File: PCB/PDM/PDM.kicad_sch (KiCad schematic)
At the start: 11 parts, among them IC4 TS5A21366DCUR, IC5 TMP126NDCKR, IC6 TMP126NDCKR, U2 MCP2561-E-SN, U3 MCP2561-E-SN

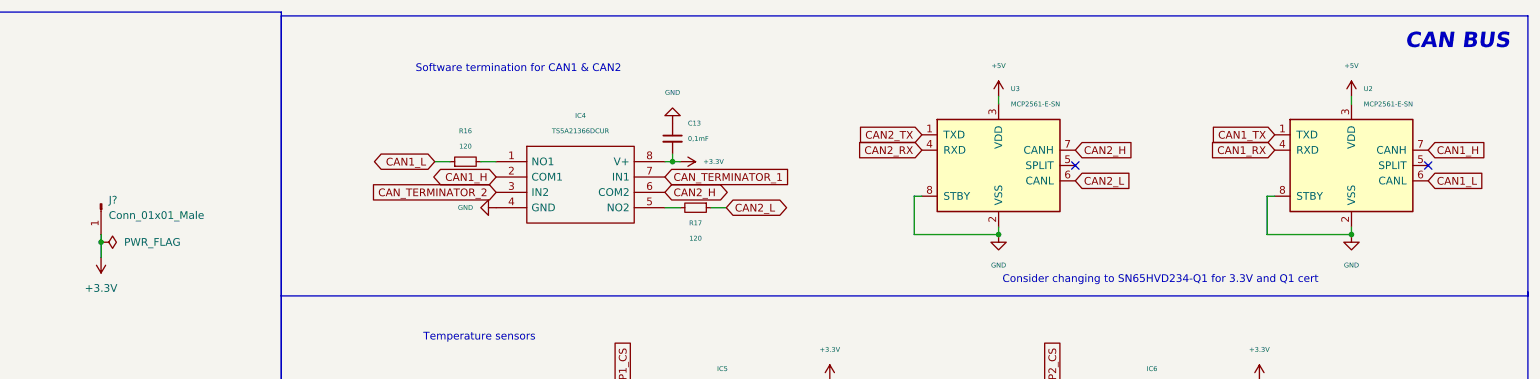
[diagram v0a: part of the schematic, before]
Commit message: Changed MCP2561 to SN65HVD230 for Q1 and 3.3V supply
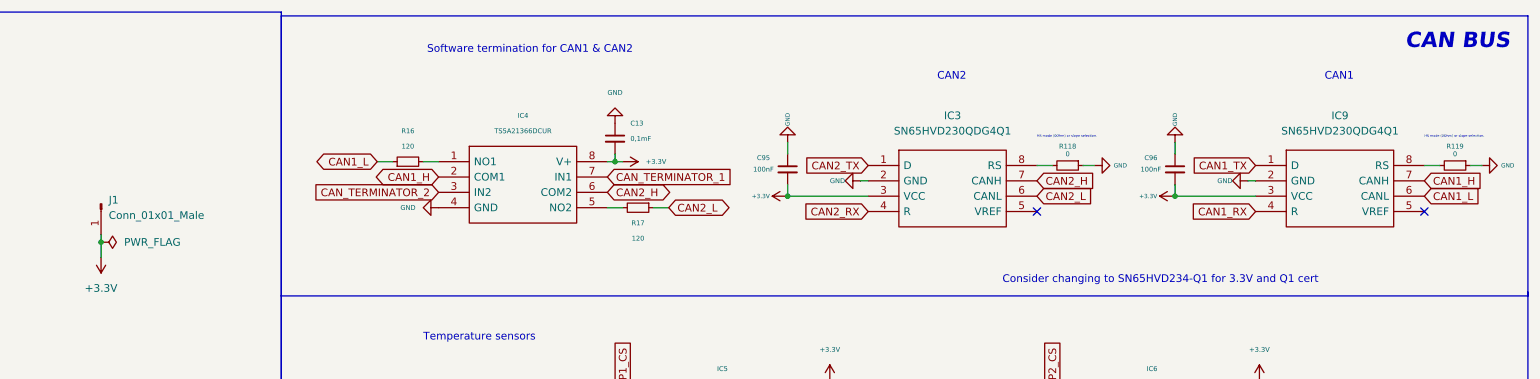
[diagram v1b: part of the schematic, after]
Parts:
- removed U2, U3: MCP2561-E-SN, Package_SO:SOIC-8_3.9x4.9mm_P1.27mm, symbol Interface_CAN_LIN:MCP2561-E-SN
- added C95, C96: 100nF, Capacitor_SMD:C_0805_2012Metric, symbol Device:C_Small
- added IC3, IC9: SN65HVD230QDG4Q1, PDM_Additional:SOIC127P600X175-8N, symbol PDM_additional:SN65HVD230QDG4Q1
- added R118, R119: 0, Resistor_SMD:R_0402_1005Metric, symbol Device:R_Small
- gave numbers to parts that had none: 1
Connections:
- net +3.3V: now also C95.2, C96.2, IC3.3 (VCC), IC9.3 (VCC)
- net CAN1_H: now also IC9.7 (CANH)
- net CAN1_L: now also IC9.6 (CANL)
- net CAN1_RX: now also IC9.4 (R)
- net CAN1_TX: now also IC9.1 (D)
- net CAN2_H: now also IC3.7 (CANH)
- net CAN2_L: now also IC3.6 (CANL)
- net CAN2_RX: now also IC3.4 (R)
- net CAN2_TX: now also IC3.1 (D)
- net GND: now also C95.1, C96.1, IC3.2 (GND), IC9.2 (GND), R118.1, R119.1
- new net: IC3.8 (RS), R118.2
- new net: IC9.8 (RS), R119.2
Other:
- note added: "CAN1"
- note added: "CAN2"
- note added: "HS mode (0Ohm) or slope selection."
- moved on the sheet: C13, IC4, R16, R17

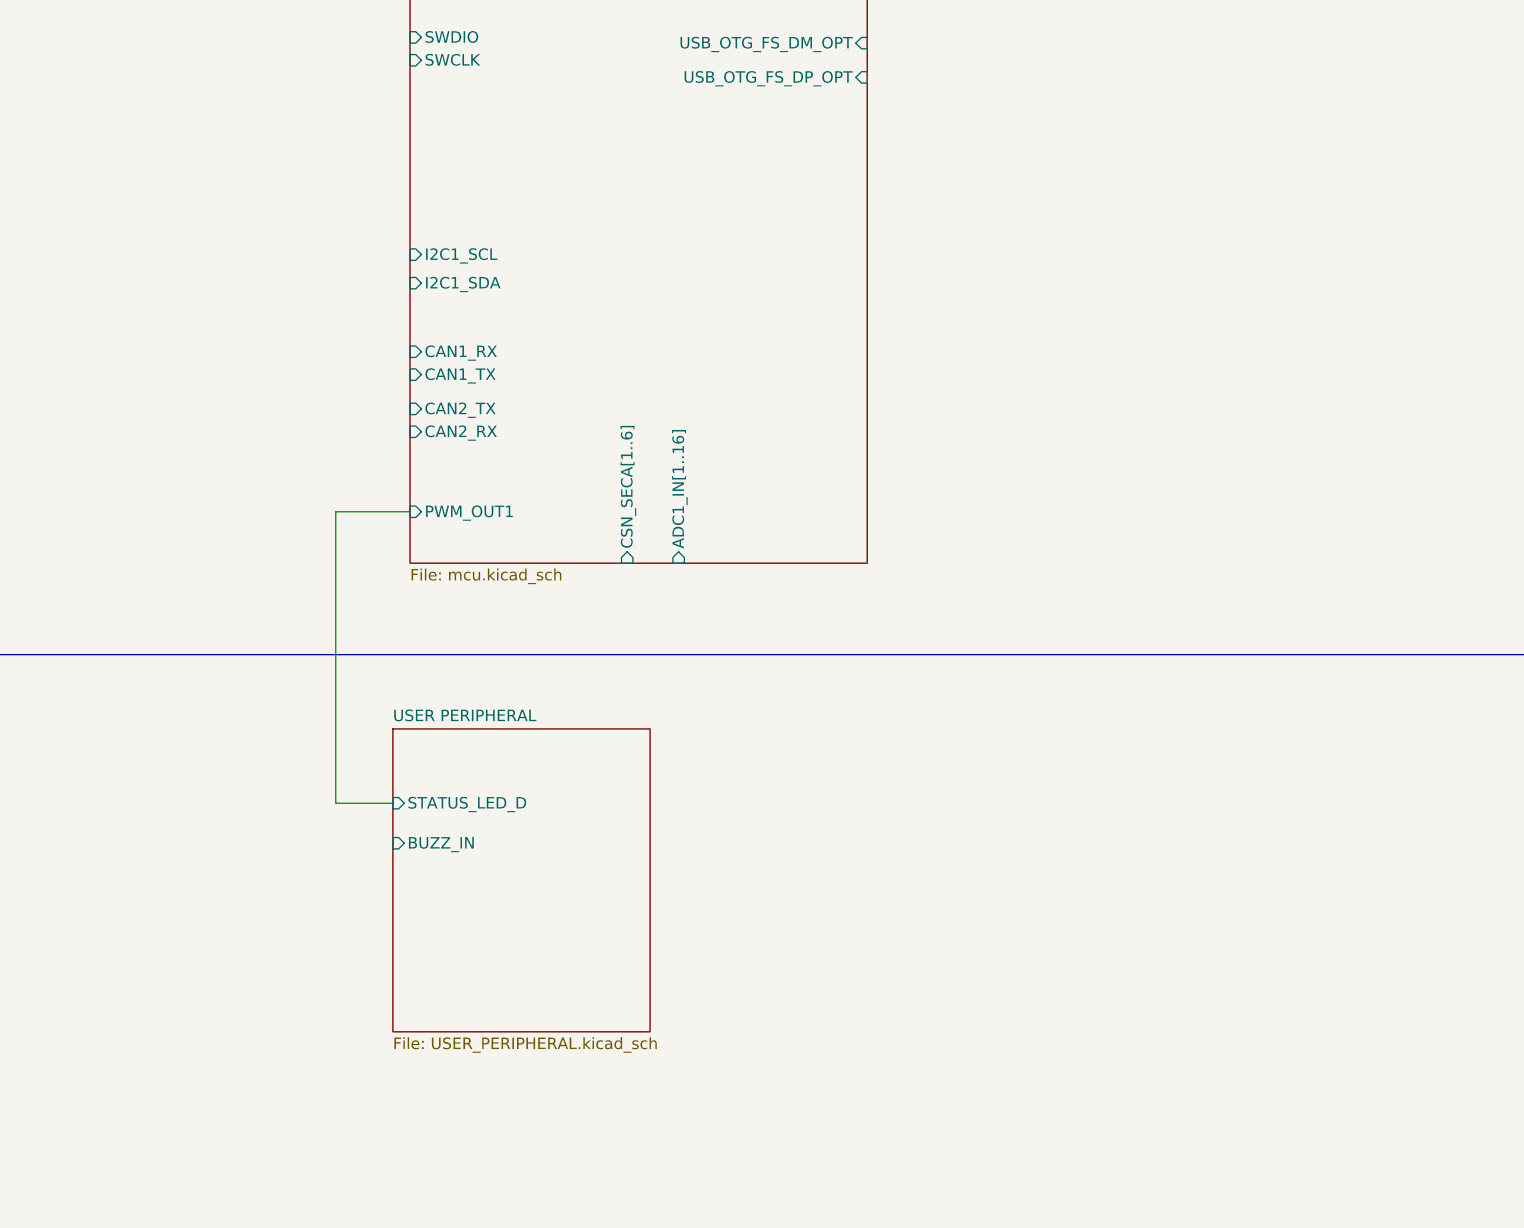
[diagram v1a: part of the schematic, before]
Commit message: Added TE Superseal 1.0 connector 60 pins
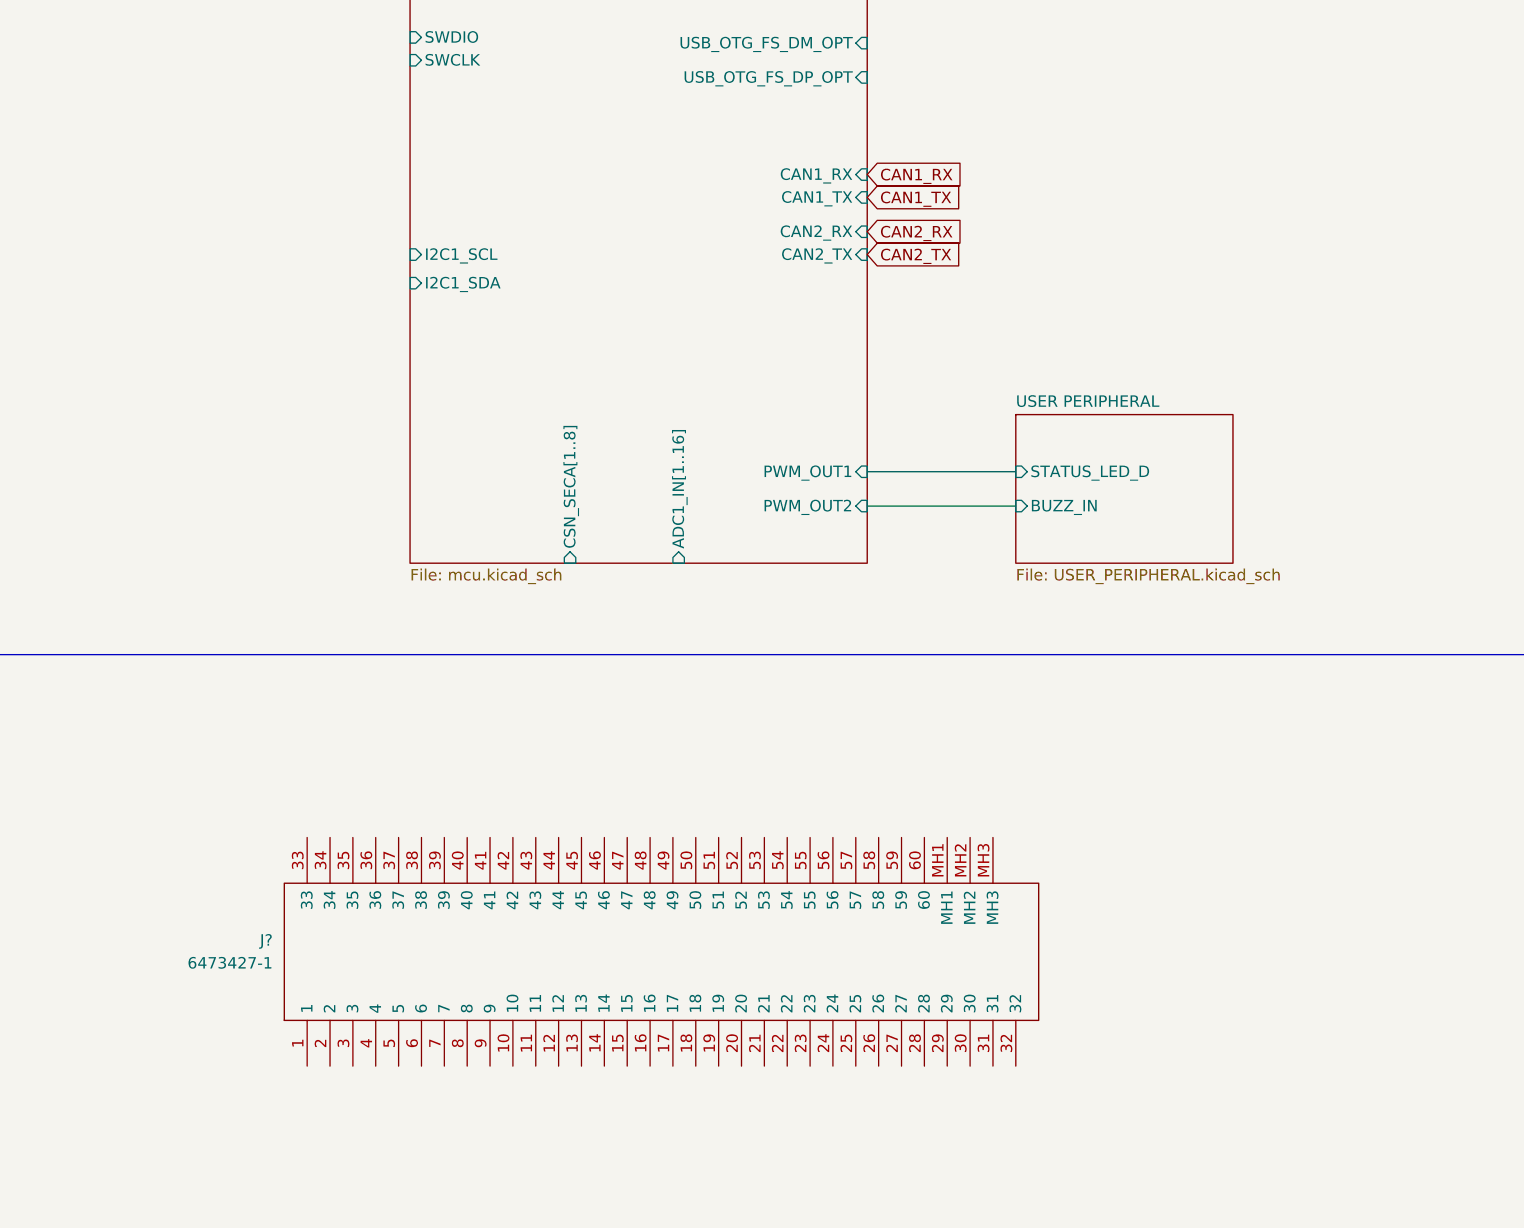
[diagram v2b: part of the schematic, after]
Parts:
- added J?: 6473427-1, 64734271, symbol PDM_additional:6473427-1
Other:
- sheet MCU ports: added CSN_SECA[1..8], PWM_OUT2; removed CSN_SECA[1..6]
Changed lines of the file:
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@@
+    (stroke (width 0) (type default) (color 0 0 0 0))
+  )
+  (wire (pts (xy 326.39 168.91) (xy 342.9 168.91))
     (stroke (width 0) (type default) (color 0 0 0 0))
   )
@@
     (stroke (width 0) (type default) (color 0 0 0 0))
   )
+  (wire (pts (xy 326.39 172.72) (xy 342.9 172.72))
+    (stroke (width 0) (type default) (color 0 0 0 0))
+  )
   (polyline (pts (xy 407.67 103.505) (xy 407.67 57.785))
     (stroke (width 0) (type default) (color 0 0 0 0))
@@
     (stroke (width 0) (type default) (color 0 0 0 0))
   )
-  (wire (pts (xy 273.685 205.74) (xy 267.335 205.74))
-    (stroke (width 0) (type default) (color 0 0 0 0))
-  )
   (wire (pts (xy 48.895 38.735) (xy 60.96 38.735))
     (stroke (width 0) (type default) (color 0 0 0 0))
@@
     (stroke (width 0) (type default) (color 0 0 0 0))
   )
-  (wire (pts (xy 267.335 205.74) (xy 267.335 173.355))
-    (stroke (width 0) (type default) (color 0 0 0 0))
-  )
   (polyline (pts (xy 201.295 285.115) (xy 12.065 285.115))
     (stroke (width 0) (type default) (color 0 0 0 0))
@@
   )
   (polyline (pts (xy 201.295 189.23) (xy 407.67 189.23))
-    (stroke (width 0) (type default) (color 0 0 0 0))
-  )
-  (wire (pts (xy 267.335 173.355) (xy 275.59 173.355))
     (stroke (width 0) (type default) (color 0 0 0 0))
   )
@@
     )
   )
+  (global_label "CAN2_RX" (shape input) (at 326.39 142.24 0) (fields_autoplaced)
+    (effects (font (size 1.27 1.27)) (justify left))
+    (property "Intersheet References" "${INTERSHEET_REFS}" (id 0) (at 337.1488 142.3194 0)
+      (effects (font (size 1.27 1.27)) (justify left) hide)
+    )
+  )
   (global_label "TEMP2_ALERT" (shape input) (at 367.03 81.28 0) (fields_autoplaced)
     (effects (font (size 1.27 1.27)) (justify left))
     (property "Intersheet References" "${INTERSHEET_REFS}" (id 0) (at 381.9617 81.2006 0)
+      (effects (font (size 1.27 1.27)) (justify left) hide)
+    )
+  )
+  (global_label "CAN1_TX" (shape input) (at 326.39 138.43 0) (fields_autoplaced)
+    (effects (font (size 1.27 1.27)) (justify left))
+    (property "Intersheet References" "${INTERSHEET_REFS}" (id 0) (at 336.8464 138.5094 0)
       (effects (font (size 1.27 1.27)) (justify left) hide)
     )
@@
     )
   )
+  (global_label "CAN1_RX" (shape input) (at 326.39 135.89 0) (fields_autoplaced)
+    (effects (font (size 1.27 1.27)) (justify left))
+    (property "Intersheet References" "${INTERSHEET_REFS}" (id 0) (at 337.1488 135.9694 0)
+      (effects (font (size 1.27 1.27)) (justify left) hide)
+    )
+  )
   (global_label "CAN1_TX" (shape input) (at 362.585 36.83 180) (fields_autoplaced)
     (effects (font (size 1.27 1.27)) (justify right))
@@
     (effects (font (size 1.27 1.27)) (justify left))
     (property "Intersheet References" "${INTERSHEET_REFS}" (id 0) (at 310.8417 81.2006 0)
+      (effects (font (size 1.27 1.27)) (justify left) hide)
+    )
+  )
+  (global_label "CAN2_TX" (shape input) (at 326.39 144.78 0) (fields_autoplaced)
+    (effects (font (size 1.27 1.27)) (justify left))
+    (property "Intersheet References" "${INTERSHEET_REFS}" (id 0) (at 336.8464 144.8594 0)
       (effects (font (size 1.27 1.27)) (justify left) hide)
     )
@@
     (pin "2")
   )
+  (symbol (lib_id "PDM_additional:6473427-1") (at 264.16 234.95 90) (unit 1)
+    (in_bom yes) (on_board yes) (fields_autoplaced)
+    (property "Reference" "J?" (id 0) (at 260.35 220.9799 90)
+      (effects (font (size 1.27 1.27)) (justify left))
+    )
+    (property "Value" "6473427-1" (id 1) (at 260.35 223.5199 90)
+      (effects (font (size 1.27 1.27)) (justify left))
+    )
+    (property "Footprint" "64734271" (id 2) (at 261.62 213.36 0)
+      (effects (font (size 1.27 1.27)) (justify left) hide)
+    )
+    (property "Datasheet" "https://www.te.com/commerce/DocumentDelivery/DDEController?Action=showdoc&DocId=Customer+Drawing%7F9-1437287-8%7FA1%7Fpdf%7FEnglish%7FENG_CD_9-1437287-8_A1.pdf%7F6473427-1" (id 3) (at 264.16 213.36 0)
+      (effects (font (size 1.27 1.27)) (justify left) hide)
+    )
+    (property "Description" "Automotive Connectors SUPER SEAL 60POS CAP ASY H AU" (id 4) (at 266.7 213.36 0)
+      (effects (font (size 1.27 1.27)) (justify left) hide)
+    )
+    (property "Height" "27.4" (id 5) (at 269.24 213.36 0)
+      (effects (font (size 1.27 1.27)) (justify left) hide)
+    )
+    (property "Manufacturer_Name" "TE Connectivity" (id 6) (at 271.78 213.36 0)
+      (effects (font (size 1.27 1.27)) (justify left) hide)
+    )
+    (property "Manufacturer_Part_Number" "6473427-1" (id 7) (at 274.32 213.36 0)
+      (effects (font (size 1.27 1.27)) (justify left) hide)
+    )
+    (property "Mouser Part Number" "571-6473427-1" (id 8) (at 276.86 213.36 0)
+      (effects (font (size 1.27 1.27)) (justify left) hide)
+    )
+    (property "Mouser Price/Stock" "https://www.mouser.co.uk/ProductDetail/TE-Connectivity/6473427-1?qs=%252BJ%252BJwDEtia0S2ZPotWhzbA%3D%3D" (id 9) (at 279.4 213.36 0)
+      (effects (font (size 1.27 1.27)) (justify left) hide)
+    )
+    (property "Arrow Part Number" "6473427-1" (id 10) (at 281.94 213.36 0)
+      (effects (font (size 1.27 1.27)) (justify left) hide)
+    )
+    (property "Arrow Price/Stock" "https://www.arrow.com/en/products/6473427-1/te-connectivity?region=nac" (id 11) (at 284.48 213.36 0)
+      (effects (font (size 1.27 1.27)) (justify left) hide)
+    )
+    (property "Mouser Testing Part Number" "" (id 12) (at 287.02 213.36 0)
+      (effects (font (size 1.27 1.27)) (justify left) hide)
+    )
+    (property "Mouser Testing Price/Stock" "" (id 13) (at 289.56 213.36 0)
+      (effects (font (size 1.27 1.27)) (justify left) hide)
+    )
+    (pin "1")
+    (pin "10")
+    (pin "11")
+    (pin "12")
+    (pin "13")
+    (pin "14")
+    (pin "15")
+    (pin "16")
+    (pin "17")
+    (pin "18")
+    (pin "19")
+    (pin "2")
+    (pin "20")
+    (pin "21")
+    (pin "22")
+    (pin "23")
+    (pin "24")
+    (pin "25")
+    (pin "26")
+    (pin "27")
+    (pin "28")
+    (pin "29")
+    (pin "3")
+    (pin "30")
+    (pin "31")
+    (pin "32")
+    (pin "33")
+    (pin "34")
+    (pin "35")
+    (pin "36")
+    (pin "37")
+    (pin "38")
+    (pin "39")
+    (pin "4")
+    (pin "40")
+    (pin "41")
+    (pin "42")
+    (pin "43")
+    (pin "44")
+    (pin "45")
+    (pin "46")
+    (pin "47")
+    (pin "48")
+    (pin "49")
+    (pin "5")
+    (pin "50")
+    (pin "51")
+    (pin "52")
+    (pin "53")
+    (pin "54")
+    (pin "55")
+    (pin "56")
+    (pin "57")
+    (pin "58")
+    (pin "59")
+    (pin "6")
+    (pin "60")
+    (pin "7")
+    (pin "8")
+    (pin "9")
+    (pin "MH1")
+    (pin "MH2")
+    (pin "MH3")
+  )
   (symbol (lib_id "power:PWR_FLAG") (at 171.45 49.53 270) (unit 1)
     (in_bom yes) (on_board yes) (fields_autoplaced)
@@
     )
   )
-  (sheet (at 273.685 197.485) (size 28.575 33.655) (fields_autoplaced)
+  (sheet (at 342.9 162.56) (size 24.13 16.51) (fields_autoplaced)
     (stroke (width 0.1524) (type solid) (color 0 0 0 0))
     (fill (color 0 0 0 0.0000))
-    (property "Sheet name" "USER PERIPHERAL" (id 0) (at 273.685 196.7734 0)
+    (property "Sheet name" "USER PERIPHERAL" (id 0) (at 342.9 161.8484 0)
       (effects (font (size 1.27 1.27)) (justify left bottom))
     )
-    (property "Sheet file" "USER_PERIPHERAL.kicad_sch" (id 1) (at 273.685 231.7246 0)
+    (property "Sheet file" "USER_PERIPHERAL.kicad_sch" (id 1) (at 342.9 179.6546 0)
       (effects (font (size 1.27 1.27)) (justify left top))
     )
-    (pin "STATUS_LED_D" input (at 273.685 205.74 180)
-      (effects (font (size 1.27 1.27)) (justify left))
-    )
-    (pin "BUZZ_IN" input (at 273.685 210.185 180)
+    (pin "STATUS_LED_D" input (at 342.9 168.91 180)
+      (effects (font (size 1.27 1.27)) (justify left))
+    )
+    (pin "BUZZ_IN" input (at 342.9 172.72 180)
       (effects (font (size 1.27 1.27)) (justify left))
     )
@@
       (effects (font (size 1.27 1.27)) (justify left))
     )
-    (pin "CAN1_RX" input (at 275.59 155.575 180)
-      (effects (font (size 1.27 1.27)) (justify left))
+    (pin "CAN1_RX" input (at 326.39 135.89 0)
+      (effects (font (size 1.27 1.27)) (justify right))
     )
     (pin "ADC1_IN[1..16]" input (at 305.435 179.07 270)
       (effects (font (size 1.27 1.27)) (justify left))
     )
-    (pin "CAN1_TX" input (at 275.59 158.115 180)
-      (effects (font (size 1.27 1.27)) (justify left))
-    )
-    (pin "CAN2_TX" input (at 275.59 161.925 180)
-      (effects (font (size 1.27 1.27)) (justify left))
-    )
-    (pin "CAN2_RX" input (at 275.59 164.465 180)
-      (effects (font (size 1.27 1.27)) (justify left))
-    )
-    (pin "PWM_OUT1" input (at 275.59 173.355 180)
-      (effects (font (size 1.27 1.27)) (justify left))
-    )
-    (pin "CSN_SECA[1..6]" input (at 299.72 179.07 270)
-      (effects (font (size 1.27 1.27)) (justify left))
+    (pin "CAN1_TX" input (at 326.39 138.43 0)
+      (effects (font (size 1.27 1.27)) (justify right))
+    )
+    (pin "CAN2_TX" input (at 326.39 144.78 0)
+      (effects (font (size 1.27 1.27)) (justify right))
+    )
+    (pin "CAN2_RX" input (at 326.39 142.24 0)
+      (effects (font (size 1.27 1.27)) (justify right))
+    )
+    (pin "PWM_OUT1" input (at 326.39 168.91 0)
+      (effects (font (size 1.27 1.27)) (justify right))
+    )
+    (pin "CSN_SECA[1..8]" input (at 293.37 179.07 270)
+      (effects (font (size 1.27 1.27)) (justify left))
+    )
+    (pin "PWM_OUT2" input (at 326.39 172.72 0)
+      (effects (font (size 1.27 1.27)) (justify right))
     )
   )
@@
       (reference "J1") (unit 1) (value "Conn_01x01_Male") (footprint "")
     )
+    (path "/ec3ef24a-d14e-4473-a6de-a99822874369"
+      (reference "J?") (unit 1) (value "6473427-1") (footprint "64734271")
+    )
     (path "/f9c327f1-1acc-4362-b996-4cc92af6a1f0/f8c11e5d-bead-478c-a036-ba63a8f5504e"
